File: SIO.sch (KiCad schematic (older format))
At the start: 16 parts, among them U10 Z84C40, U11 SP232E, U12 SP232E

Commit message: Assign footprints to schematic, drawing custom connector, socket, and switch footprints as needed.
git-svn-id: svn+ssh://dev.thehead.ca/depot/main/z80@617 995eaefb-0ce2-40e3-b8bc-69bf8729875b
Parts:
- C12, C13, C14, C15, C16, C17, C18, C19, C21, C22, C23: footprint (none) -> Capacitors_THT:C_Disc_D4.3mm_W1.9mm_P5.00mm
- SER1, SER2: footprint (none) -> z80_footprints:L717SDE09P1ACH
- U10: footprint (none) -> Housings_DIP:DIP-40_W15.24mm_Socket_LongPads
- U11, U12: footprint (none) -> Housings_DIP:DIP-16_W7.62mm_LongPads
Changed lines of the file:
@@
 Sheet 4 7
 Title "Serial Ports"
-Date "2018-03-28"
-Rev "6"
+Date "2018-04-11"
+Rev "7"
 Comp ""
 Comment1 ""
@@
 F 0 "U10" H 3750 3991 50  0000 L TNN
 F 1 "Z84C40" H 4550 4000 50  0000 R TNN
-F 2 "" H 4550 4000 60  0001 C CNN
+F 2 "Housings_DIP:DIP-40_W15.24mm_Socket_LongPads" H 4550 4000 60  0001 C CNN
 F 3 "" H 4550 4000 60  0001 C CNN
 	1    4150 2900
@@
 F 0 "U11" H 6350 3475 50  0000 R CNN
 F 1 "SP232E" H 6350 3400 50  0000 R CNN
-F 2 "" H 6500 1300 50  0001 L CNN
+F 2 "Housings_DIP:DIP-16_W7.62mm_LongPads" H 6500 1300 50  0001 L CNN
 F 3 "" H 6450 2450 50  0001 C CNN
 	1    6450 2350
@@
 F 0 "U12" H 6350 6325 50  0000 R CNN
 F 1 "SP232E" H 6350 6250 50  0000 R CNN
-F 2 "" H 6500 4150 50  0001 L CNN
+F 2 "Housings_DIP:DIP-16_W7.62mm_LongPads" H 6500 4150 50  0001 L CNN
 F 3 "" H 6450 5300 50  0001 C CNN
 	1    6450 5200
@@
 F 0 "C12" H 5675 1700 50  0000 L CNN
 F 1 "0.1uF" H 5675 1500 50  0000 L CNN
-F 2 "" H 5688 1450 50  0001 C CNN
+F 2 "Capacitors_THT:C_Disc_D4.3mm_W1.9mm_P5.00mm" H 5688 1450 50  0001 C CNN
 F 3 "" H 5650 1600 50  0001 C CNN
 	1    5650 1600
@@
 F 0 "C17" H 7575 2500 50  0000 L CNN
 F 1 "0.1uF" H 7575 2300 50  0000 L CNN
-F 2 "" H 7588 2250 50  0001 C CNN
+F 2 "Capacitors_THT:C_Disc_D4.3mm_W1.9mm_P5.00mm" H 7588 2250 50  0001 C CNN
 F 3 "" H 7550 2400 50  0001 C CNN
 	1    7550 2400
@@
 F 0 "C14" H 7275 1700 50  0000 L CNN
 F 1 "0.1uF" H 7275 1500 50  0000 L CNN
-F 2 "" H 7288 1450 50  0001 C CNN
+F 2 "Capacitors_THT:C_Disc_D4.3mm_W1.9mm_P5.00mm" H 7288 1450 50  0001 C CNN
 F 3 "" H 7250 1600 50  0001 C CNN
 	1    7250 1600
@@
 F 0 "C16" H 7575 1900 50  0000 L CNN
 F 1 "0.1uF" H 7575 1700 50  0000 L CNN
-F 2 "" H 7588 1650 50  0001 C CNN
+F 2 "Capacitors_THT:C_Disc_D4.3mm_W1.9mm_P5.00mm" H 7588 1650 50  0001 C CNN
 F 3 "" H 7550 1800 50  0001 C CNN
 	1    7550 1800
@@
 F 0 "C19" H 7575 5350 50  0000 L CNN
 F 1 "0.1uF" H 7575 5150 50  0000 L CNN
-F 2 "" H 7588 5100 50  0001 C CNN
+F 2 "Capacitors_THT:C_Disc_D4.3mm_W1.9mm_P5.00mm" H 7588 5100 50  0001 C CNN
 F 3 "" H 7550 5250 50  0001 C CNN
 	1    7550 5250
@@
 F 0 "C15" H 7275 4550 50  0000 L CNN
 F 1 "0.1uF" H 7275 4350 50  0000 L CNN
-F 2 "" H 7288 4300 50  0001 C CNN
+F 2 "Capacitors_THT:C_Disc_D4.3mm_W1.9mm_P5.00mm" H 7288 4300 50  0001 C CNN
 F 3 "" H 7250 4450 50  0001 C CNN
 	1    7250 4450
@@
 F 0 "C18" H 7575 4750 50  0000 L CNN
 F 1 "0.1uF" H 7575 4550 50  0000 L CNN
-F 2 "" H 7588 4500 50  0001 C CNN
+F 2 "Capacitors_THT:C_Disc_D4.3mm_W1.9mm_P5.00mm" H 7588 4500 50  0001 C CNN
 F 3 "" H 7550 4650 50  0001 C CNN
 	1    7550 4650
@@
 F 0 "C13" H 5675 4550 50  0000 L CNN
 F 1 "0.1uF" H 5675 4350 50  0000 L CNN
-F 2 "" H 5688 4300 50  0001 C CNN
+F 2 "Capacitors_THT:C_Disc_D4.3mm_W1.9mm_P5.00mm" H 5688 4300 50  0001 C CNN
 F 3 "" H 5650 4450 50  0001 C CNN
 	1    5650 4450
@@
 F 0 "SER1" H 8400 3450 50  0000 C CNN
 F 1 "DB9-M" H 8400 3375 50  0000 C CNN
-F 2 "" H 8400 2800 50  0001 C CNN
+F 2 "z80_footprints:L717SDE09P1ACH" H 8400 2800 50  0001 C CNN
 F 3 "" H 8400 2800 50  0001 C CNN
 	1    8400 2800
@@
 F 0 "SER2" H 8400 6300 50  0000 C CNN
 F 1 "DB9-M" H 8400 6225 50  0000 C CNN
-F 2 "" H 8400 5650 50  0001 C CNN
+F 2 "z80_footprints:L717SDE09P1ACH" H 8400 5650 50  0001 C CNN
 F 3 "" H 8400 5650 50  0001 C CNN
 	1    8400 5650
@@
 F 0 "C21" H 4275 7350 50  0000 L CNN
 F 1 "0.1uF" H 4275 7150 50  0000 L CNN
-F 2 "" H 4288 7100 50  0001 C CNN
+F 2 "Capacitors_THT:C_Disc_D4.3mm_W1.9mm_P5.00mm" H 4288 7100 50  0001 C CNN
 F 3 "" H 4250 7250 50  0001 C CNN
 	1    4250 7250
@@
 F 0 "C22" H 4575 7350 50  0000 L CNN
 F 1 "0.1uF" H 4575 7150 50  0000 L CNN
-F 2 "" H 4588 7100 50  0001 C CNN
+F 2 "Capacitors_THT:C_Disc_D4.3mm_W1.9mm_P5.00mm" H 4588 7100 50  0001 C CNN
 F 3 "" H 4550 7250 50  0001 C CNN
 	1    4550 7250
@@
 F 0 "C23" H 4875 7350 50  0000 L CNN
 F 1 "0.1uF" H 4875 7150 50  0000 L CNN
-F 2 "" H 4888 7100 50  0001 C CNN
+F 2 "Capacitors_THT:C_Disc_D4.3mm_W1.9mm_P5.00mm" H 4888 7100 50  0001 C CNN
 F 3 "" H 4850 7250 50  0001 C CNN
 	1    4850 7250

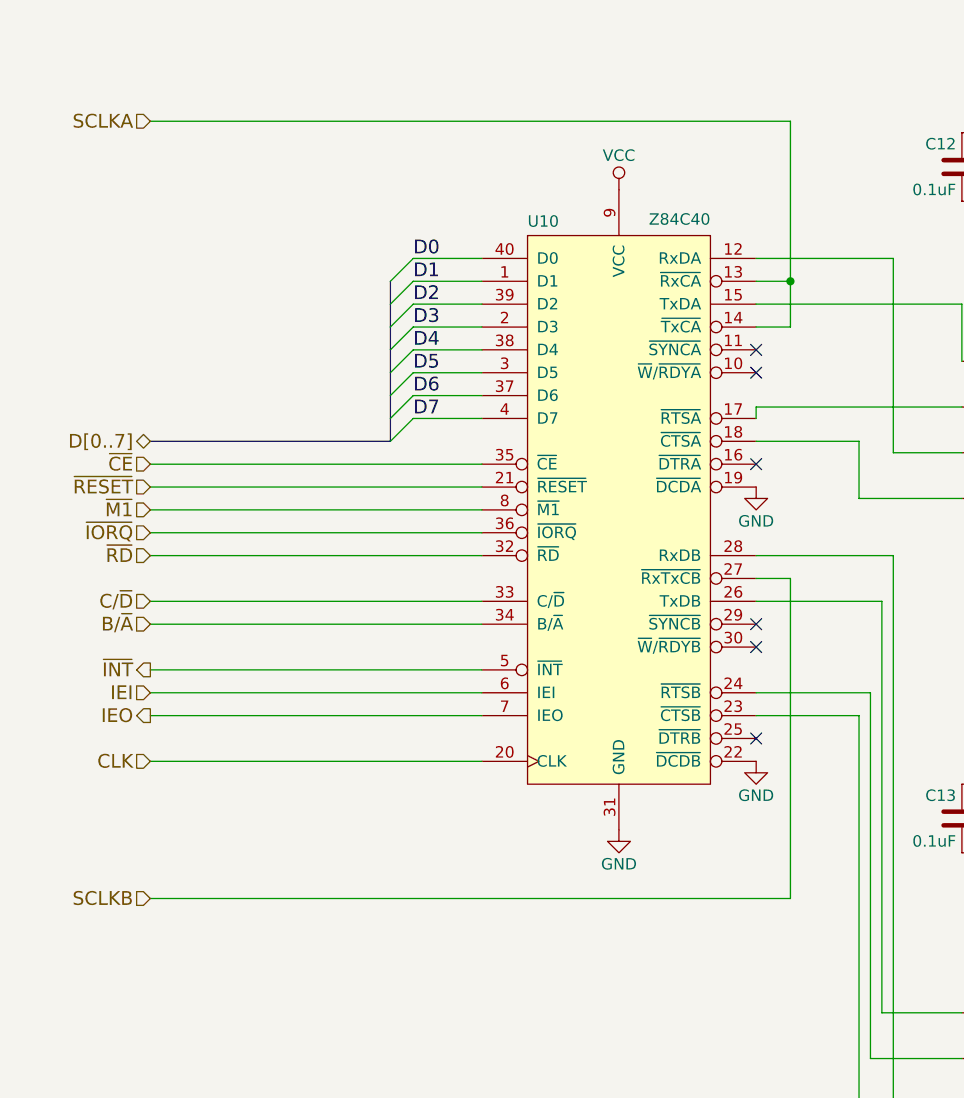
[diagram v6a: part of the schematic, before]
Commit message: Schematic for an LCD panel interface circuit.
git-svn-id: svn+ssh://dev.thehead.ca/depot/main/z80@632 995eaefb-0ce2-40e3-b8bc-69bf8729875b
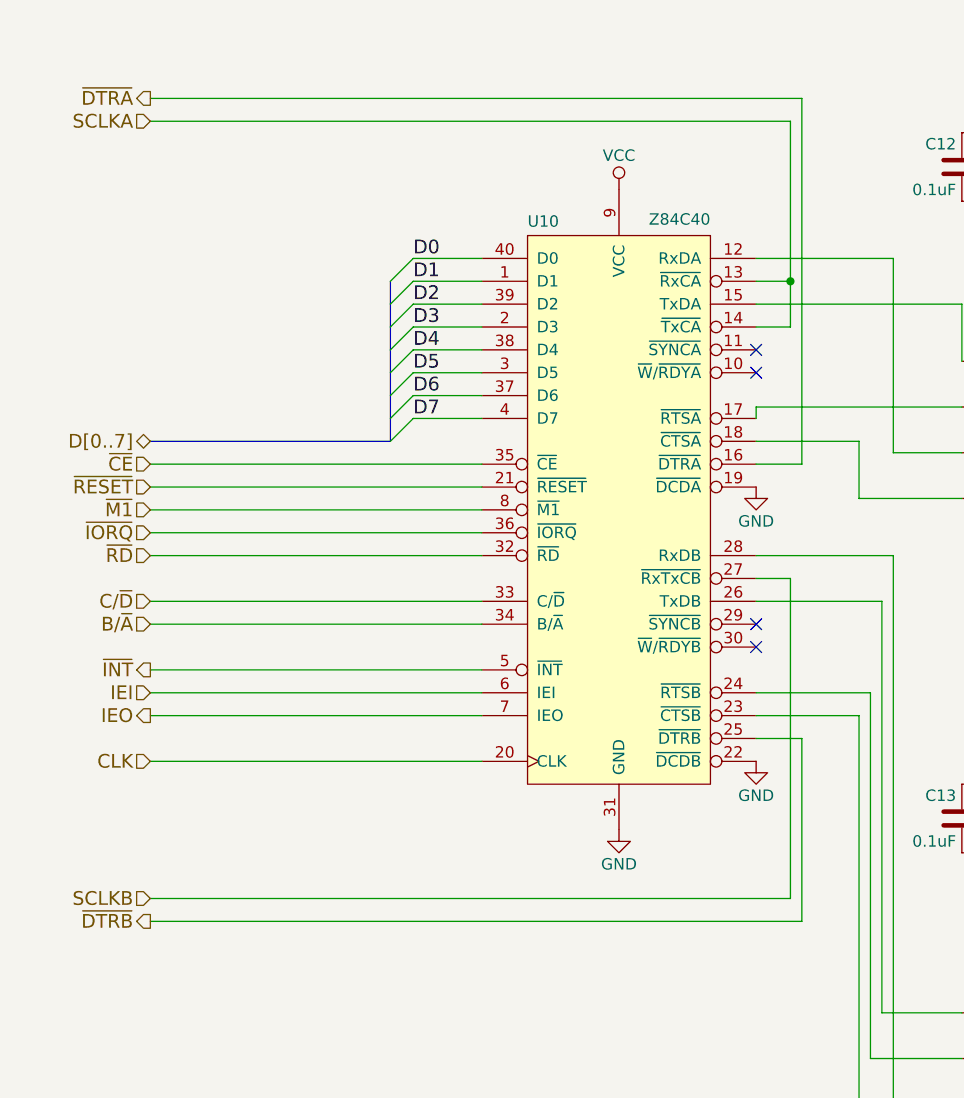
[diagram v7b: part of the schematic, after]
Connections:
- net ~DTRA: now reaches U10.16 (~DTRA)
- net ~DTRB: now reaches U10.25 (~DTRB)
- no-connect marks 14 -> 12
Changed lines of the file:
@@
 $Descr USLetter 11000 8500
 encoding utf-8
-Sheet 4 7
+Sheet 4 8
 Title "Serial Ports"
-Date "2018-06-12"
-Rev "10"
+Date "2018-07-18"
+Rev "11"
 Comp ""
 Comment1 ""
@@
 $EndComp
 $Comp
-L GND #PWR037
+L GND #PWR039
 U 1 1 59D787F7
 P 4150 4500
-F 0 "#PWR037" H 4150 4250 50  0001 C CNN
+F 0 "#PWR039" H 4150 4250 50  0001 C CNN
 F 1 "GND" H 4150 4350 50  0000 C CNN
 F 2 "" H 4150 4500 50  0001 C CNN
@@
 $EndComp
 $Comp
-L VCC #PWR038
+L VCC #PWR040
 U 1 1 59D787FD
 P 4150 1700
-F 0 "#PWR038" H 4150 1550 50  0001 C CNN
+F 0 "#PWR040" H 4150 1550 50  0001 C CNN
 F 1 "VCC" H 4150 1850 50  0000 C CNN
 F 2 "" H 4150 1700 50  0001 C CNN
@@
 $EndComp
 $Comp
-L GND #PWR039
+L GND #PWR041
 U 1 1 59D78845
 P 6450 3550
-F 0 "#PWR039" H 6450 3300 50  0001 C CNN
+F 0 "#PWR041" H 6450 3300 50  0001 C CNN
 F 1 "GND" H 6450 3400 50  0000 C CNN
 F 2 "" H 6450 3550 50  0001 C CNN
@@
 $EndComp
 $Comp
-L VCC #PWR040
+L VCC #PWR042
 U 1 1 59D7884B
 P 6450 1150
-F 0 "#PWR040" H 6450 1000 50  0001 C CNN
+F 0 "#PWR042" H 6450 1000 50  0001 C CNN
 F 1 "VCC" H 6450 1300 50  0000 C CNN
 F 2 "" H 6450 1150 50  0001 C CNN
@@
 $EndComp
 $Comp
-L GND #PWR041
+L GND #PWR043
 U 1 1 59D7885B
 P 4750 3000
-F 0 "#PWR041" H 4750 2750 50  0001 C CNN
+F 0 "#PWR043" H 4750 2750 50  0001 C CNN
 F 1 "GND" H 4750 2850 50  0000 C CNN
 F 2 "" H 4750 3000 50  0001 C CNN
@@
 	1    0    0    -1
 $EndComp
-NoConn ~ 4750 2900
-$Comp
-L GND #PWR042
+$Comp
+L GND #PWR044
 U 1 1 59D78862
 P 4750 4200
-F 0 "#PWR042" H 4750 3950 50  0001 C CNN
+F 0 "#PWR044" H 4750 3950 50  0001 C CNN
 F 1 "GND" H 4750 4050 50  0000 C CNN
 F 2 "" H 4750 4200 50  0001 C CNN
@@
 	1    0    0    -1
 $EndComp
-NoConn ~ 4750 4100
 $Comp
 L MAX232 U12
@@
 $EndComp
 $Comp
-L GND #PWR043
+L GND #PWR045
 U 1 1 59D78870
 P 6450 6400
-F 0 "#PWR043" H 6450 6150 50  0001 C CNN
+F 0 "#PWR045" H 6450 6150 50  0001 C CNN
 F 1 "GND" H 6450 6250 50  0000 C CNN
 F 2 "" H 6450 6400 50  0001 C CNN
@@
 $EndComp
 $Comp
-L VCC #PWR044
+L VCC #PWR046
 U 1 1 59D78876
 P 6450 4000
-F 0 "#PWR044" H 6450 3850 50  0001 C CNN
+F 0 "#PWR046" H 6450 3850 50  0001 C CNN
 F 1 "VCC" H 6450 4150 50  0000 C CNN
 F 2 "" H 6450 4000 50  0001 C CNN
@@
 $EndComp
 $Comp
-L GND #PWR045
+L GND #PWR047
 U 1 1 59D7889D
 P 7550 2550
-F 0 "#PWR045" H 7550 2300 50  0001 C CNN
+F 0 "#PWR047" H 7550 2300 50  0001 C CNN
 F 1 "GND" H 7550 2400 50  0000 C CNN
 F 2 "" H 7550 2550 50  0001 C CNN
@@
 $EndComp
 $Comp
-L VCC #PWR046
+L VCC #PWR048
 U 1 1 59D788AC
 P 7550 1650
-F 0 "#PWR046" H 7550 1500 50  0001 C CNN
+F 0 "#PWR048" H 7550 1500 50  0001 C CNN
 F 1 "VCC" H 7550 1800 50  0000 C CNN
 F 2 "" H 7550 1650 50  0001 C CNN
@@
 $EndComp
 $Comp
-L GND #PWR047
+L GND #PWR049
 U 1 1 59D788C0
 P 7550 5400
-F 0 "#PWR047" H 7550 5150 50  0001 C CNN
+F 0 "#PWR049" H 7550 5150 50  0001 C CNN
 F 1 "GND" H 7550 5250 50  0000 C CNN
 F 2 "" H 7550 5400 50  0001 C CNN
@@
 $EndComp
 $Comp
-L VCC #PWR048
+L VCC #PWR050
 U 1 1 59D788CF
 P 7550 4500
-F 0 "#PWR048" H 7550 4350 50  0001 C CNN
+F 0 "#PWR050" H 7550 4350 50  0001 C CNN
 F 1 "VCC" H 7550 4650 50  0000 C CNN
 F 2 "" H 7550 4500 50  0001 C CNN
@@
 $EndComp
 $Comp
-L GND #PWR049
+L GND #PWR051
 U 1 1 59D788EF
 P 7950 2400
-F 0 "#PWR049" H 7950 2150 50  0001 C CNN
+F 0 "#PWR051" H 7950 2150 50  0001 C CNN
 F 1 "GND" H 7950 2250 50  0000 C CNN
 F 2 "" H 7950 2400 50  0001 C CNN
@@
 $EndComp
 $Comp
-L GND #PWR050
+L GND #PWR052
 U 1 1 59D78907
 P 7950 5250
-F 0 "#PWR050" H 7950 5000 50  0001 C CNN
+F 0 "#PWR052" H 7950 5000 50  0001 C CNN
 F 1 "GND" H 7950 5100 50  0000 C CNN
 F 2 "" H 7950 5250 50  0001 C CNN
@@
 NoConn ~ 4750 3600
 $Comp
-L GND #PWR051
+L GND #PWR053
 U 1 1 59D7891A
 P 8400 3400
-F 0 "#PWR051" H 8400 3150 50  0001 C CNN
+F 0 "#PWR053" H 8400 3150 50  0001 C CNN
 F 1 "GND" H 8400 3250 50  0000 C CNN
 F 2 "" H 8400 3400 50  0001 C CNN
@@
 $EndComp
 $Comp
-L GND #PWR052
+L GND #PWR054
 U 1 1 59D78920
 P 8400 6250
-F 0 "#PWR052" H 8400 6000 50  0001 C CNN
+F 0 "#PWR054" H 8400 6000 50  0001 C CNN
 F 1 "GND" H 8400 6100 50  0000 C CNN
 F 2 "" H 8400 6250 50  0001 C CNN
@@
 B/~A
 $Comp
-L GND #PWR053
+L GND #PWR055
 U 1 1 59D81D49
 P 3700 7400
-F 0 "#PWR053" H 3700 7150 50  0001 C CNN
+F 0 "#PWR055" H 3700 7150 50  0001 C CNN
 F 1 "GND" H 3700 7250 50  0000 C CNN
 F 2 "" H 3700 7400 50  0001 C CNN
@@
 $EndComp
 $Comp
-L VCC #PWR054
+L VCC #PWR056
 U 1 1 59D81D56
 P 3700 7100
-F 0 "#PWR054" H 3700 6950 50  0001 C CNN
+F 0 "#PWR056" H 3700 6950 50  0001 C CNN
 F 1 "VCC" H 3700 7250 50  0000 C CNN
 F 2 "" H 3700 7100 50  0001 C CNN
@@
 Text HLabel 2100 4800 0    60   Input ~ 0
 SCLKB
+Text HLabel 2100 1300 0    60   Output ~ 0
+~DTRA
+Wire Wire Line
+	2100 1300 4950 1300
+Wire Wire Line
+	4950 1300 4950 2900
+Wire Wire Line
+	4950 2900 4750 2900
+Text HLabel 2100 4900 0    60   Output ~ 0
+~DTRB
+Wire Wire Line
+	4750 4100 4950 4100
+Wire Wire Line
+	4950 4100 4950 4900
+Wire Wire Line
+	4950 4900 2100 4900
 $EndSCHEMATC
